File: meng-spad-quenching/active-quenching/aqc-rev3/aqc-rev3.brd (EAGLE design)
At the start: 120 x 74.9 mm, 284 parts, among them IC1 TPS7A4901, IC10 LT1534-1, IC11 HFA3134, IC12 HFA3134, IC13 HFA3134, IC14 LTC1711, IC15 NC7SV74K8X, IC16 74AHC1G14DCK, IC17 NL17SZ125, IC18 74AHC1G04DCK, IC19 74AHC1G32DCK, IC2 TPS7A4901, IC20 NC7WZ16P6X, IC21 74AHC1G08DCK, IC22 74AHC1G08DCK, IC23 HFA3134, IC24 TLV272DGK, IC25 THAT320, IC26 TLV272DGK, IC27 HFA3134, IC28 TLV271DBV, IC29 USBLC6-2SC6Y, IC3 LT1534-1, IC30 STM32F411RE, IC31 MAX572X, IC32 LM1117, IC4 ADCMP582, IC5 HFA3134, IC6 HFA3135, IC7 DS1100LU-20+, IC8 HFA3135, IC9 TPS7A3001, M1 BSS806N, M2 BSS806N, Q1 IRLML6402TRPBF, SW1 MCU_RST, T1 MMBTH10, U1 MCP4725, U2 SN65EPT22DGK, U3 SN65EPT21DGK, X1 CONN_PULLDN_SENSE, X2 CONN_FORCE_QUENCH, X3 KEYSTONE-7774, X4 CONN_SPAD, X5 CONN_PHOTON_COUNTER, X6 KEYSTONE-7774, X7 CONN_SMU, X8 PN61729-S

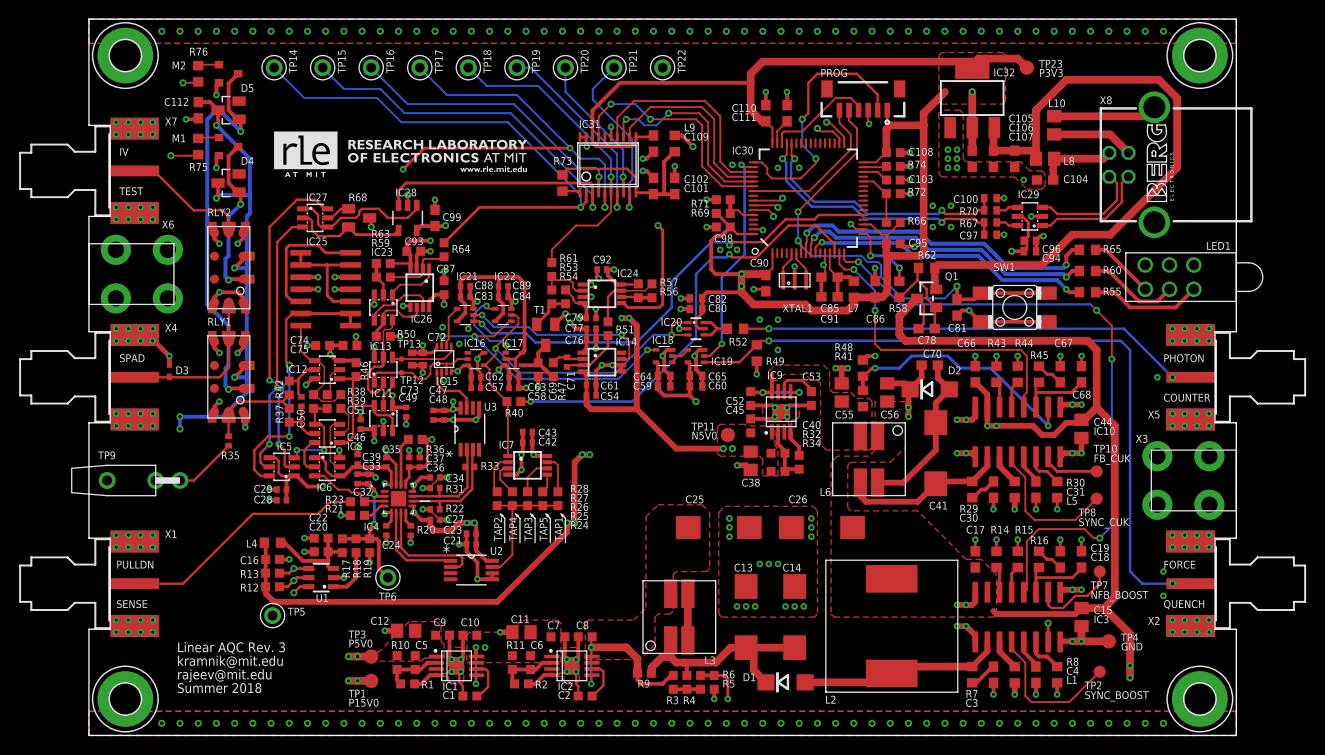
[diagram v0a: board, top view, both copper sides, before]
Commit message: Fixed silkscreen errors
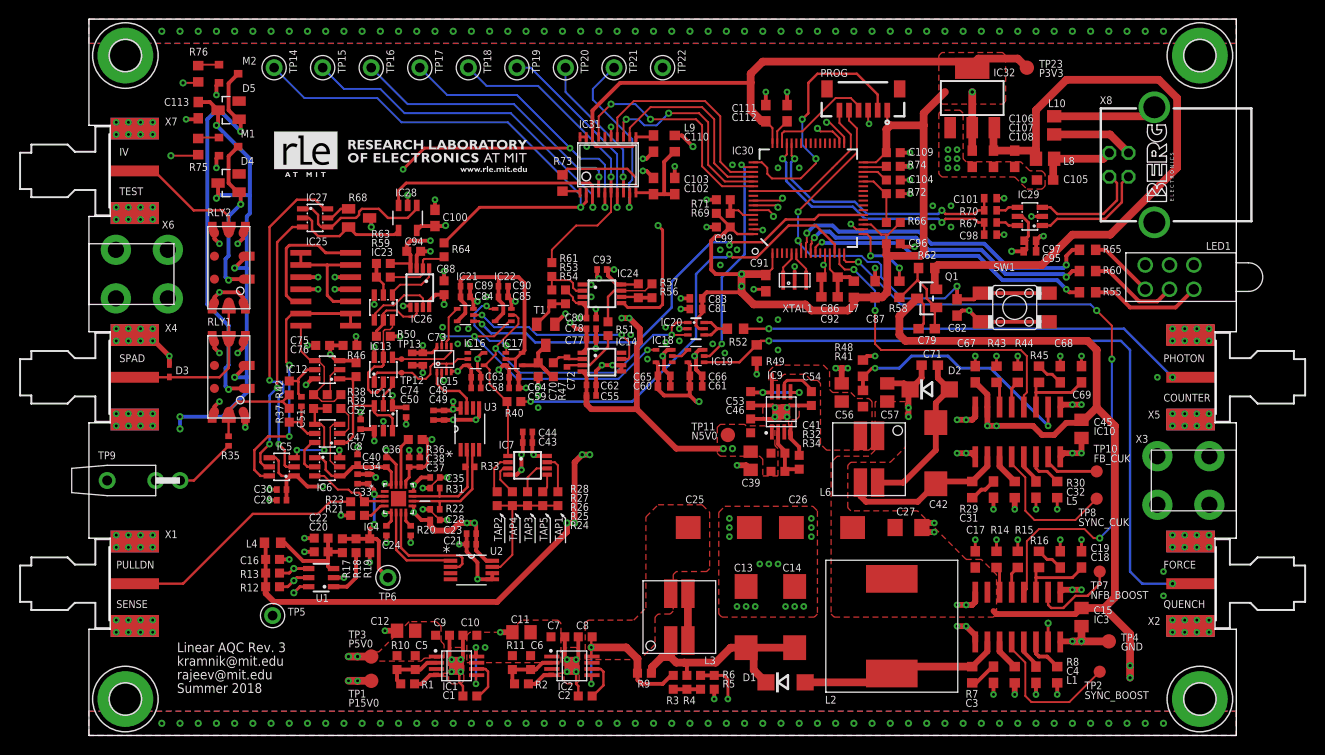
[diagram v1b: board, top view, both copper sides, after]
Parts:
- added C113: 100n, rcl:C0603
- C100: value 47p -> 100n; device rcl:C0402 -> rcl:C0603
- C101: value 100n -> 47p; device rcl:C0603 -> rcl:C0402
- C102, C107: value 4u7 -> 100n
- C103, C108, C87: value 100n -> 4u7; device rcl-modified-footprints:C0603 -> rcl:C0603
- C104: value 10n -> 100n; device rcl:C0603 -> rcl-modified-footprints:C0603
- C105, C28, C34, C48, C52, C60, C75: value 100n -> 10n
- C109, C99: device rcl:C0603 -> rcl-modified-footprints:C0603
- C27: value 10n -> 10u; device rcl-modified-footprints:C0402 -> rcl:C1206
- C29, C33, C37, C43, C49, C53, C65, C73, C77: value 10n -> 100n
- C30, C90: device rcl:C0603 -> rcl-modified-footprints:C0402
- C31: value 1300p -> 10n
- C32: value 100n -> 1300p; device rcl-modified-footprints:C0402 -> rcl:C0603
- C38: value 10u -> 10n; device rcl:C0805 -> rcl-modified-footprints:C0402
- C39: value 10n -> 10u; device rcl-modified-footprints:C0402 -> rcl:C0805
- C40, C93: device rcl-modified-footprints:C0603 -> rcl-modified-footprints:C0402
- C41: value 68u, 16V -> 10n; device rcl:CT7343 -> rcl-modified-footprints:C0603
- C42: value 100n -> 68u, 16V; device rcl-modified-footprints:C0402 -> rcl:CT7343
- C44: value 4u7 -> 10n; device rcl:C0805 -> rcl-modified-footprints:C0402
- C45: value 100n -> 4u7; device rcl-modified-footprints:C0603 -> rcl:C0805
- C46: value 10n -> 100n; device rcl-modified-footprints:C0402 -> rcl-modified-footprints:C0603
- C50: value 100p -> 10n
- C51: value 10n -> 100p; device rcl-modified-footprints:C0603 -> rcl-modified-footprints:C0402
- C54: value 100n -> 10n; device rcl-modified-footprints:C0402 -> rcl-modified-footprints:C0603
- C55: value 10u, 10V -> 100n; device rcl:C0805 -> rcl-modified-footprints:C0402
- C56: value 4u7 -> 10u, 10V
- C57: value 100n -> 4u7; device rcl-modified-footprints:C0402 -> rcl:C0805
- C59, C80: value 10n -> 100n; device rcl:C0402 -> rcl-modified-footprints:C0402
- C61, C83: value 10n -> 100n; device rcl-modified-footprints:C0402 -> rcl:C0402
- C64: value 100n -> 10n; device rcl:C0402 -> rcl-modified-footprints:C0402
- C66: value 100n -> 10n; device rcl:C0603 -> rcl:C0402
- C67: value 33n -> 100n
- C68: value DNP -> 33n
- C69: value 100p -> DNP; device rcl-modified-footprints:C0603 -> rcl:C0603
- C70: value DNP -> 100p; device rcl:C0603 -> rcl-modified-footprints:C0603
- C71, C79, C92: device rcl-modified-footprints:C0402 -> rcl:C0603
- C72: value 100n -> DNP; device rcl:C0402 -> rcl-modified-footprints:C0402
- C74, C95: device rcl-modified-footprints:C0603 -> rcl:C0402
- C76, C88: device rcl-modified-footprints:C0402 -> rcl-modified-footprints:C0603
- C78: value 100n -> 10n; device rcl:C0603 -> rcl-modified-footprints:C0402
- C81: device rcl:C0603 -> rcl:C0402
- C82: value 100n -> 10n; device rcl:C0402 -> rcl:C0603
- C85: value 4u7 -> 10n; device rcl:C0603 -> rcl-modified-footprints:C0402
- C94: device rcl:C0402 -> rcl-modified-footprints:C0603
- C96: value 10n -> 100n; device rcl:C0402 -> rcl-modified-footprints:C0603
- C97: value 47p -> 10n
- C98: value 100n -> 47p; device rcl-modified-footprints:C0603 -> rcl:C0402
- moved C30 74.5 mm to (20.2, 25.7), turned to 180 degrees
- moved C32 71.0 mm to (99.1, 25.7), turned to 270 degrees
- moved C94 64.5 mm to (34.0, 50.6)
- moved C112 61.6 mm to (73.0, 65.1), turned to 90 degrees
- moved C100 58.1 mm to (36.2, 54.1), turned to 90 degrees
- moved C44 57.9 mm to (45.9, 31.8), turned to 180 degrees
- moved C69 56.8 mm to (103.8, 37.8), turned to 90 degrees
- moved C27 49.5 mm to (85.7, 21.7)
- moved C52 45.7 mm to (23.5, 34.9)
- moved C87 45.1 mm to (82.2, 46.7)
- moved C40 44.0 mm to (28.1, 28.9), turned to 90 degrees
- moved C57 43.0 mm to (83.5, 35.9), turned to 90 degrees
- moved C42 42.7 mm to (88.6, 29.5), turned to 90 degrees
- moved C39 41.1 mm to (69.2, 28.7), turned to 270 degrees
- moved C70 41.0 mm to (47.0, 38.3), turned to 270 degrees
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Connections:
- net DIAMOND_IBIAS_BOTTOM: now also C52.2; no longer C51.2
- net DIAMOND_IBIAS_TOP: now also C52.1; no longer C51.1
- net DMD_OP_NPN: now also C51.1; no longer C50.1
- net DMD_OP_PNP: now also C51.2; no longer C50.2
- net GND: now also C113.2, C40.2, C50.2, C71.2, C78.2; no longer C42.2, C52.2, C72.2, C79.2
- net LDO_N10V0_FB_CH1: now also C41.2; no longer C40.2
- net LDO_N10V0_NR_SS_CH1: now also C54.1; no longer C53.1
- net MCU_NRST: now also C82.1; no longer C81.1
- net MCU_PB11: now also C104.1; no longer C103.1
- net MCU_USB_FS_D_N: now also C101.1; no longer C100.1
- net MCU_USB_FS_D_P: now also C98.1; no longer C97.1
- net MCU_VCAP_2: now also C112.1; no longer C111.1
- net N$11: now also C72.2; no longer C71.2
- net N$12: now also C79.1; no longer C78.1
- net N$13: now also C72.1; no longer C71.1
- net N$62: now also C31.1; no longer C30.1
- net N$63: now also C68.1; no longer C67.1
- net N$64: now also C69.1; no longer C68.1
- net N$68: now also C42.+; no longer C41.+
- net N$69: now also C42.-, C71.1; no longer C41.-, C70.1
- net N$8: now also C32.1; no longer C31.1
- net ONE_SHOT_CAP: now also C70.1; no longer C69.1
- net PP_N5V0_ANALOG: now also C39.1, C41.1, C46.1, C55.1, C62.1, C80.1, C94.1; no longer C36.1, C40.1, C45.1, C54.1, C61.1, C79.1, C93.1
- net PP_N6V0_CUK: now also C53.1, C56.1; no longer C52.1, C55.1
- net PP_P15V0_ANALOG: now also C76.1; no longer C74.1
- net PP_P3V3: now also C106.1, C111.1, C28.1, C35.1, C44.1, C49.1, C61.1, C66.1, C74.1, C81.1, C85.1, C87.1, C91.1, C97.1, C99.1; no longer C105.1, C108.1, C27.1, C34.1, C42.1, C47.1, C57.1, C62.1, C72.1, C80.1, C82.1, C86.1, C88.1, C94.1, C98.1
- net PP_P3V3_VDDA: now also C86.1, C92.1; no longer C85.1, C91.1
- net PP_P5V0_ANALOG: now also C100.1, C30.1, C36.1, C40.1, C47.1, C50.1, C78.1, C88.1, C93.1; no longer C28.1, C35.1, C39.1, C46.1, C49.1, C76.1, C87.1, C92.1, C99.1
- net PP_P5V0_DAC1: now also C103.1; no longer C101.1
- net SMPS_USB_VDD: now also C113.1, C27.1, C45.1, C57.1, C67.1, C79.2; no longer C112.1, C44.1, C56.1, C66.1, C78.2
- net USBCONN_P1: now also C105.1; no longer C104.1
- net USB_VDD: now also C108.1; no longer C106.1
- net VREF_AV_DET: now also C34.1; no longer C32.1
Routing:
- net GND: track 300.1 -> 303.1 mm, vias 380 -> 395

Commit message: Added renaming script and started
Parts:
- C23, C29, C33, C35, C36, C37, C43, C49, C55, C58, C59, C61, C65, C73, C77, C80, C83, C89, C90, C93, C95: value 100n -> CAP CER 0.1UF 10V X7R 0402 10%

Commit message: rev3 bom work
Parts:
- C1, C105, C2, C31, C41, C5, C52, C54, C6, C75, C82: value 10n -> CAP CER 10000PF 25V X7R 0603 10%
- C10, C100, C102, C104, C106, C107, C109, C110, C111, C112, C113, C16, C17, C20, C46, C53, C67, C7, C76, C79, C8, C88, C9, C91, C92, C94, C96, C99: value 100n -> CAP CER 0.1UF 25V X7R 0603 10%
- C101, C98: value 47p -> CAP CER 47PF 16V C0G 0402 5%
- C103, C108, C22, C86, C87: value 4u7 -> CAP CER 4.7UF 6.3V X7R 0603 10%
- C11: value 10u -> CAP CER 10UF 25V X5R 0805 10%
- C12, C39: value 10u -> CAP CER 10UF 16V X7R 0805 20%
- C13, C14, C25, C26: value 47u, 20V -> CAP ALUM POLY 47UF 20% 20V SMD
- C15, C45, C57: value 4u7 -> CAP CER 4.7UF 25V X7R 0805 10%
- C18: value 15n -> CAP CER 0.015UF 50V X7R 0603 10%
- C19: value 220p -> CAP CER 220PF 50V C0G 0603 5%
- C21, C24, C28, C30, C34, C38, C40, C44, C47, C48, C50, C60, C62, C63, C64, C66, C74, C78, C81, C84, C85, C97: value 10n -> CAP CER 10000PF 10V X7R 0402 10%
- C27: value 10u -> CAP CER 10UF 10V X7R 1206 10%
- C3: value 1n -> CAP CER 1000PF 50V X7R 0603 10%
- C32, C4: value 1300p -> CAP CER 1300PF 50V C0G 0603 5%
- C42: value 68u, 16V -> CAP ALUM POLY 68UF 20% 16V SMD
- C51: value 100p -> CAP CER 100PF 25V C0G/NP0 0402
- C56: value 10u, 10V -> CAP CER 10UF 16V X7R 0805 20%
- C68: value 33n -> CAP CER 0.033UF 50V X7R 0603 10%
- C70: value 100p -> CAP CER 100PF 50V C0G 0603 5%
- D3: value TVS -> DF2B29FU,H3F
- IC31: value MAX572X -> MAX5725
- IC7: value DS1100LU-20+ -> DS1100LU-45+
- L2: value 732-1699-2-ND -> Wurth-7447709471
- LED1: value 5640200132F -> Dialight-5640200132F
- Q1: value IRLML6402TRPBF -> DMG2305UX-13
- R1, R34: value 24k -> RES SMD 24K OHM 1% 1/10W 0603
- R10, R32: value 76k8 -> RES SMD 76.8K OHM 1% 1/10W 0603
- R11: value 137k -> RES SMD 137K OHM 1% 1/10W 0603
- R12, R13: value 2k2 -> RES SMD 2.2K OHM 1% 1/10W 0603
- R14, R15, R18, R43, R44, R48: value 1k -> RES SMD 1K OHM 1% 1/10W 0603
- R16: value 6k8 -> RES SMD 6.8K OHM 1% 1/10W 0603
- R2: value 11k8 -> RES SMD 11.8K OHM 1% 1/10W 0603
- R20, R35: value 49R9 -> RES SMD 49.9 OHM 1% 1/10W 0402
- R22, R31: value 150R -> RES SMD 150 OHM 1% 1/10W 0402
- R23, R46: value 220R, 1% -> RES SMD 220 OHM 1% 1/10W 0603
- R29, R75, R76: value 100R -> RES SMD 100 OHM 1% 1/8W 0603
- R3, R47, R51, R71, R73, R74: value 0R -> RES SMD 0 OHM JUMPER 0603
- R30, R8: value 16k9 -> RES SMD 16.9K OHM 1% 1/10W 0603
- R33: value 100R -> RES SMD 100 OHM 1% 1/10W 0402
- R36, R54: value 10k -> RES SMD 10K OHM 1% 1/10W 0603
- R37, R42: value 100R, 1% -> RES SMD 100 OHM 1% 1/8W 0603
- R38, R39: value 200R, 1% -> RES SMD 200 OHM 1% 1/10W 0603
- R40, R49, R52: value 49R9 -> RES SMD 49.9 OHM 1% 1/10W 0603
- R41: value 1k4 -> RES SMD 1.4K OHM 1% 1/10W 0603
- R45: value 2k -> RES SMD 2K OHM 1% 1/10W 0603
- R5: value 29k4 -> RES SMD 29.4K OHM 1% 1/10W 0603
- R50: value 110R, 1% -> RES SMD 110 OHM 1% 1/10W 0603
- R53, R61: value 220k -> RES SMD 220K OHM 1% 1/10W 0603
- R55, R60, R65: value 470R -> RES SMD 470 OHM 1% 1/10W 0603
- R56, R57, R62: value 100k -> RES SMD 100K OHM 1% 1/10W 0603
- R58: value 4k7 -> RES SMD 4.7K OHM 1% 1/10W 0603
- R59: value 127k, 1% -> RES SMD 127K OHM 1% 1/10W 0603
- R6: value 2k49 -> RES SMD 2.49K OHM 1% 1/10W 0603
- R63: value 274R, 1% -> RES SMD 274 OHM 1% 1/10W 0603
- R64: value 102k, 1% -> RES SMD 102K OHM 1% 1/10W 0603
- R67, R70: value 22R -> RES SMD 22 OHM 1% 1/10W 0402
- R7: value 10R -> RES SMD 10 OHM 1% 1/10W 0603
- T1: value MMBTH10 -> MMBTH10−4LT1G
- X8: value PN61729-S -> 61729-0010BLF
